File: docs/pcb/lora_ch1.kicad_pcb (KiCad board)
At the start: 2 copper layers, 69 x 34.5 mm, 41 parts

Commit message: PCB rework V1.3 Removed BMS1 (FS8205A), BATTP1 (DW01A) and connected BATT- to GND. Resolved the conflict between battery and built in LDO.
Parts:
- removed BATTP1: DW01A, Package_TO_SOT_SMD:SOT-23-6
- removed BMS1: FS8205A, Package_TO_SOT_SMD:SOT-23-6
- removed C9: 0.1uF, PCM_SparkFun-Capacitor:C_0603_1608Metric
- removed R6: 100, PCM_SparkFun-Resistor:R_0603_1608Metric
- removed R7: 1k, PCM_SparkFun-Resistor:R_0603_1608Metric
- moved BATTC1 8.50 mm to (125.0, 89.5)
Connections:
- BATTC1 pad 1: BATT_MINUS -> GND
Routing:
- net BATT_MINUS: track 19.0 -> 0.00 mm, vias 2 -> 0
- net GND: track 37.5 -> 25.6 mm, vias 6 -> 22
- net Net-(BATTP1-VCC): track 8.87 -> 0.00 mm, vias 2 -> 0
- net DRV_EN: track 55.7 -> 48.5 mm
- net OC: track 6.22 -> 0.00 mm, vias 2 -> 0
- net OD: track 5.56 -> 0.00 mm, vias 2 -> 0
- net SCL: track 62.7 -> 58.3 mm
- net BATT_PLUS: track 45.7 -> 50.0 mm
- net Net-(BATTP1-CS): track 2.43 -> 0.00 mm

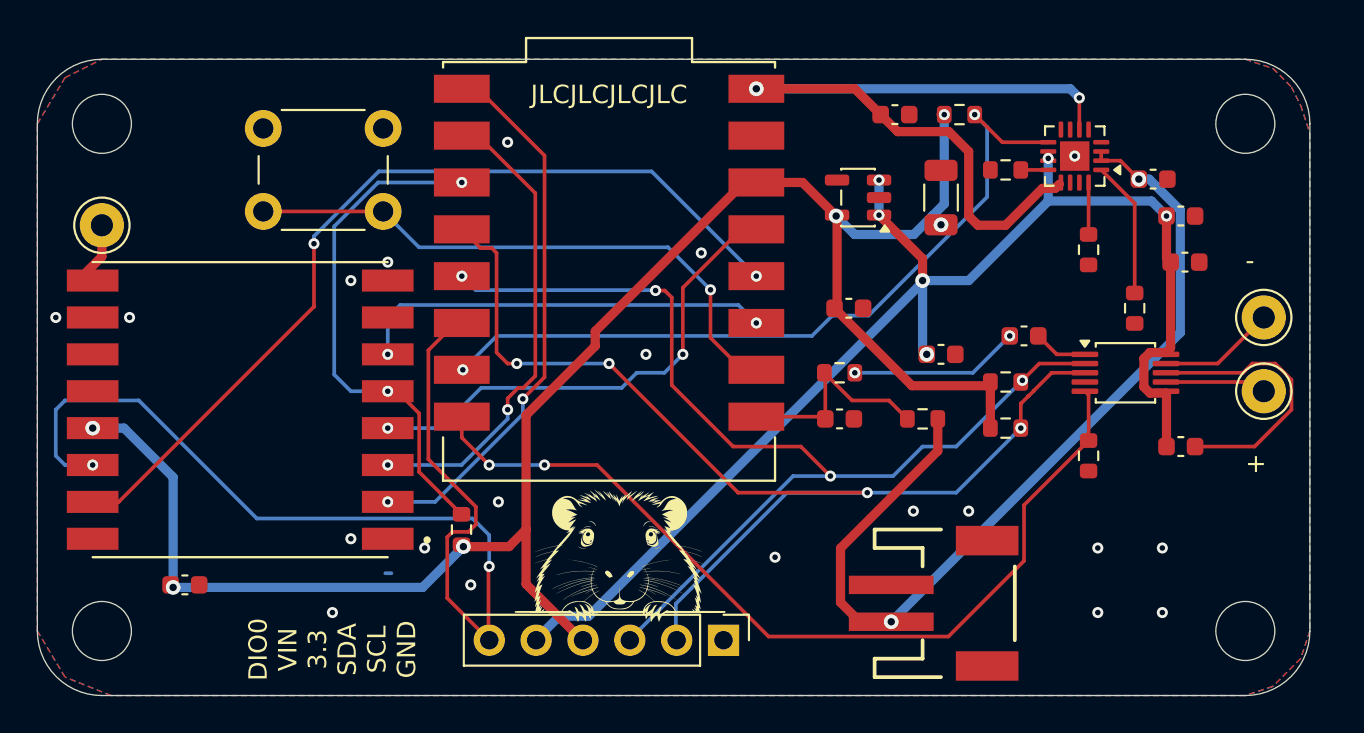
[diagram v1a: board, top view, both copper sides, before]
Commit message: SET_VIB, GET_VIB added. Editable with control char. write to change the haptics profile.
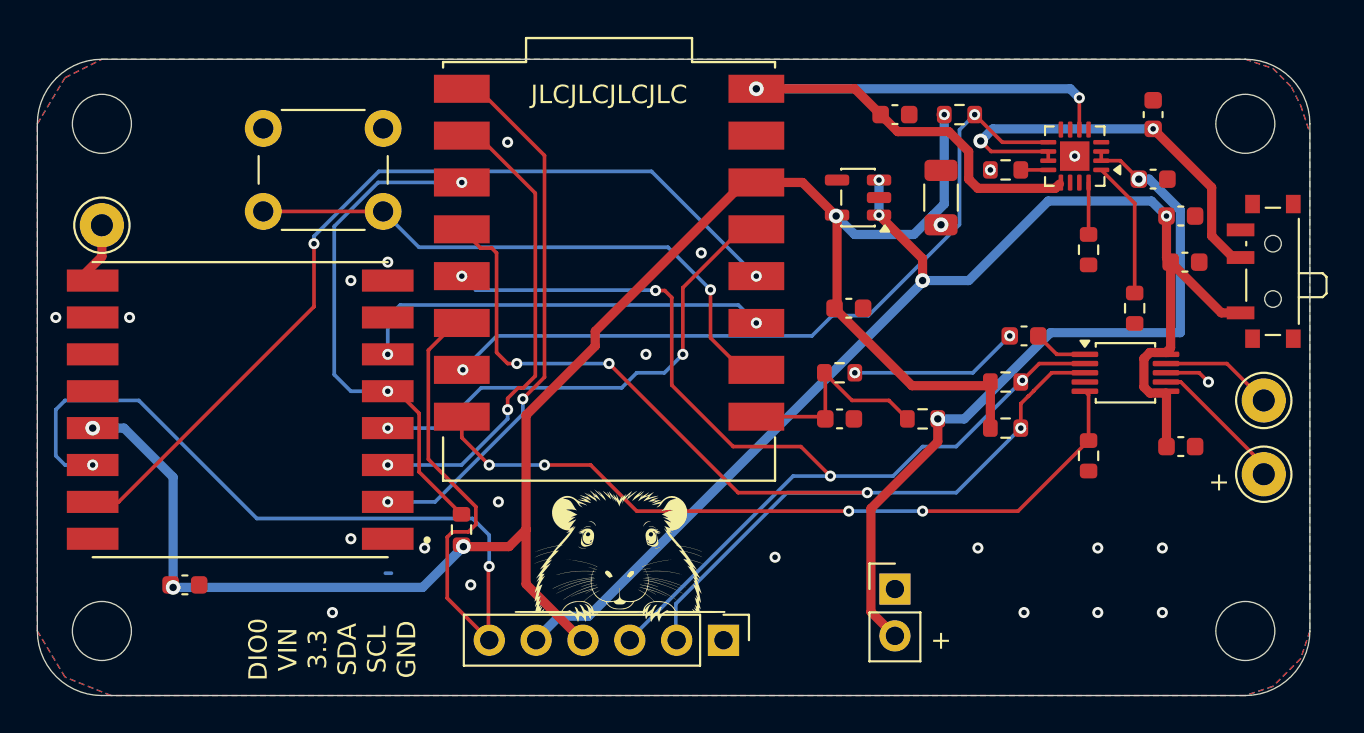
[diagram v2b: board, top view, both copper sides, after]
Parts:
- removed BATTC1: JST_2mm_LiPo, PCM_SparkFun-Connector:JST_1x02_P2.0mm_Horizontal_SMD
- added +: Conn_01x02_Pin, Connector_PinHeader_2.54mm:PinHeader_1x02_P2.54mm_Vertical, F.Cu at (121.5, 88.7)
- added SW1: SW_SPDT, Button_Switch_SMD:SW_SPDT_PCM12, F.Cu at (141.7, 71.5)
- moved C14 17.4 mm to (135.5, 63.0), turned to 90 degrees
- moved LRAM1 4.50 mm to (141.5, 78.5)
- moved LRAP1 4.50 mm to (141.5, 82.5)
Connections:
- C14 pad 1: V_IN -> SYS_PWR
- CHRG1 pad 10: V_IN -> SYS_PWR
- CHRG1 pad 11: V_IN -> SYS_PWR
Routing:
- net SYS_PWR: track 0.00 -> 23.2 mm, vias 0 -> 2
- net GND: track 25.6 -> 13.1 mm, vias 22 -> 24
- net BATT_PLUS: track 50.0 -> 41.4 mm
- net DRV_EN: track 48.5 -> 41.1 mm, vias 2 -> 4
- net V_USB: track 42.0 -> 39.2 mm
- net LRA+: track 5.51 -> 7.66 mm
- net V_IN: track 72.6 -> 70.7 mm, vias 6 -> 4
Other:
- board text removed: "-"
